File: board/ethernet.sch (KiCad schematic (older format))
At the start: 1 part

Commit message: Roughed out ethernet sheet
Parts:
- added C? (x4): 10n 200V, agg:0805, symbol C
- added C? (x5): 100n, agg:0603, symbol C
- added C? (x2): 30p, agg:0603, symbol C
- added C?: 2u2, agg:0603, symbol C
- added C? (x2): 22u, agg:1206, symbol C
- added C?: C, agg:0603, symbol C
- added C?: 100n 60V, agg:0805, symbol C
- added C? (x6): C, symbol C
- added D?: 1N4148, agg:SOD-323, symbol D
- added D? (x8): SS110B, agg:DO-214AA-SMB, symbol D
- added D?: SMAJ58A, agg:DO-214AC-SMA, symbol ZENERsmall
- added IC?: KSZ8081RNx, agg:QFN-24-EP-MICREL, symbol KSZ8081RNx
- added IC?: MAX5969x, agg:DFN-10-EP-MAX, symbol MAX5969x
- added IC?: MAX17503, agg:QFN-20-EP-MAX, symbol MAX17503
- added L?: FB, agg:0603, symbol L_Small
- added L?: 3u3, symbol INDUCTOR
- added L?: INDUCTOR, symbol INDUCTOR
- added R? (x4): 75, agg:0603, symbol R
- added R? (x4): 33, agg:0603, symbol R_Small
- added R?: 1k, agg:0603, symbol R_Small
- added R?: 6k49, agg:0603, symbol R
- added R?: 10k, agg:0603, symbol R
- added R? (x2): 1k, agg:0603, symbol R
- added R?: 24k9, agg:0603, symbol R_Small
- added R?: 619, agg:0603, symbol R_Small
- added R?: 3M3, symbol R_Small
- added R? (x2): R, symbol R
- added T?: 749010012A, agg:749010012A, symbol 749010012A
- added Y?: 25MHz, agg:XTAL-50x32, symbol Crystal
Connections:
- net +48V: now also C?.1, IC?.1 (VIN), IC?.2 (VIN), IC?.3 (VIN), L?.1, R?.1
- net CRS_DV: now also R?.1
- net MDC: now also IC?.11 (MDC)
- net MDIO: now also IC?.10 (MDIO), R?.2
- net REF_CLK: now also R?.1
- net RXD0: now also R?.1
- net RXD1: now also R?.1
- net TXD0: now also IC?.20 (TXD0)
- net TXD1: now also IC?.21 (TXD1)
- net TXEN: now also IC?.19 (TXEN)
- net at J?.1: now also T?.8 (TD+)
- net at J?.10: now also R?.2
- net TRAFFIC_LED: now reaches J?.11
- net at J?.12: now also R?.1
- net at J?.2: now also T?.6 (TD-)
- net at J?.3: now also T?.3 (RD+)
- net VB2: now reaches J?.4
- net VB2: now also J?.5, C?.1, C?.1, D?.1 (K), D?.1 (K), D?.2 (A)
- net at J?.6: now also T?.1 (RD-)
- net VB1: now reaches J?.7
- net VB1: now also J?.8, C?.1, D?.1 (K), D?.2 (A)
- net LINK_LED: now reaches J?.9
- net LINK_LED: now also IC?.23 (LED0)
- new net: C?.1, T?.10 (CTX)
- new net: IC?.5 (TXM), T?.11 (TX-)
- new net: IC?.4 (RXP), T?.14 (RX+)
- new net: C?.1, T?.15 (CRX)
- new net: IC?.3 (RXM), T?.16 (RX-)
- new net: C?.1, T?.2 (CRD)
- new net: C?.1, T?.7 (CTD)
- new net: IC?.6 (TXP), T?.9 (TX+)
- new net: C?.1, C?.1, IC?.1 (VDD_1v2)
- new net: IC?.12 (RXD1), R?.2
- new net: IC?.13 (RXD0), R?.2
- new net: IC?.15 (CRS_DV), R?.2
- new net: IC?.16 (REF_CLK), R?.2
- new net: C?.1, C?.1, IC?.2 (VDDA_3v3), L?.1
- new net: C?.1, D?.2 (A), IC?.24 (~RST), R?.2
- new net: C?.1, IC?.7 (XO), Y?.2
- new net: C?.1, IC?.8 (XI), Y?.1
- new net: IC?.9 (REXT), R?.1
- new net: D?.1 (K), D?.1 (K), D?.1 (K), D?.1 (K), IC?.1 (VDD), L?.2, R?.2
- new net: IC?.10 (CLS), R?.1
- new net: IC?.2 (DET), R?.1
- new net: C?.2, D?.2 (A), D?.2 (A), D?.2 (A), D?.2 (A), D?.2 (A), IC?.5 (VSS), IC?.EP (VSS), R?.2
- new net: C?.1, IC?.12 (VCC)
- new net: C?.2, IC?.17 (LX), IC?.18 (LX), IC?.19 (LX), L?.2
- new net: C?.1, IC?.20 (BST)
- new net: C?.1, IC?.7 (SS)
- new net: IC?.9 (FB), R?.1, R?.2
- new net: C?.2, R?.1 (x4)
- new net: R?.2, R?.2, R?.2, R?.2
- new net +12V: C?.1, C?.1, L?.1, R?.1
- new net +3V3: C?.1, C?.1, D?.1 (K), IC?.14 (VDDIO), L?.2, R?.1, R?.1, R?.1, R?.2
- new net GND: C?.2, C?.2, C?.2, C?.2, C?.2, C?.2, C?.2, C?.2, C?.2, C?.2, C?.2, C?.2, C?.2, C?.2, C?.2, C?.2, IC?.11 (MODE), IC?.13 (SGND), IC?.14 (PGND), IC?.15 (PGND), IC?.16 (PGND), IC?.22 (GND), IC?.6 (RTN), IC?.7 (WAD), IC?.EP (GND), IC?.EP (SGND), R?.2, R?.2
- new net POE_GOOD: IC?.4 (EN/UVLO), IC?.8 (PG), R?.2
- new net VA1: D?.1 (K), D?.2 (A)
- new net VA2: D?.1 (K), D?.2 (A)
- no-connect marks 0 -> 7
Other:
- moved on the sheet: J?

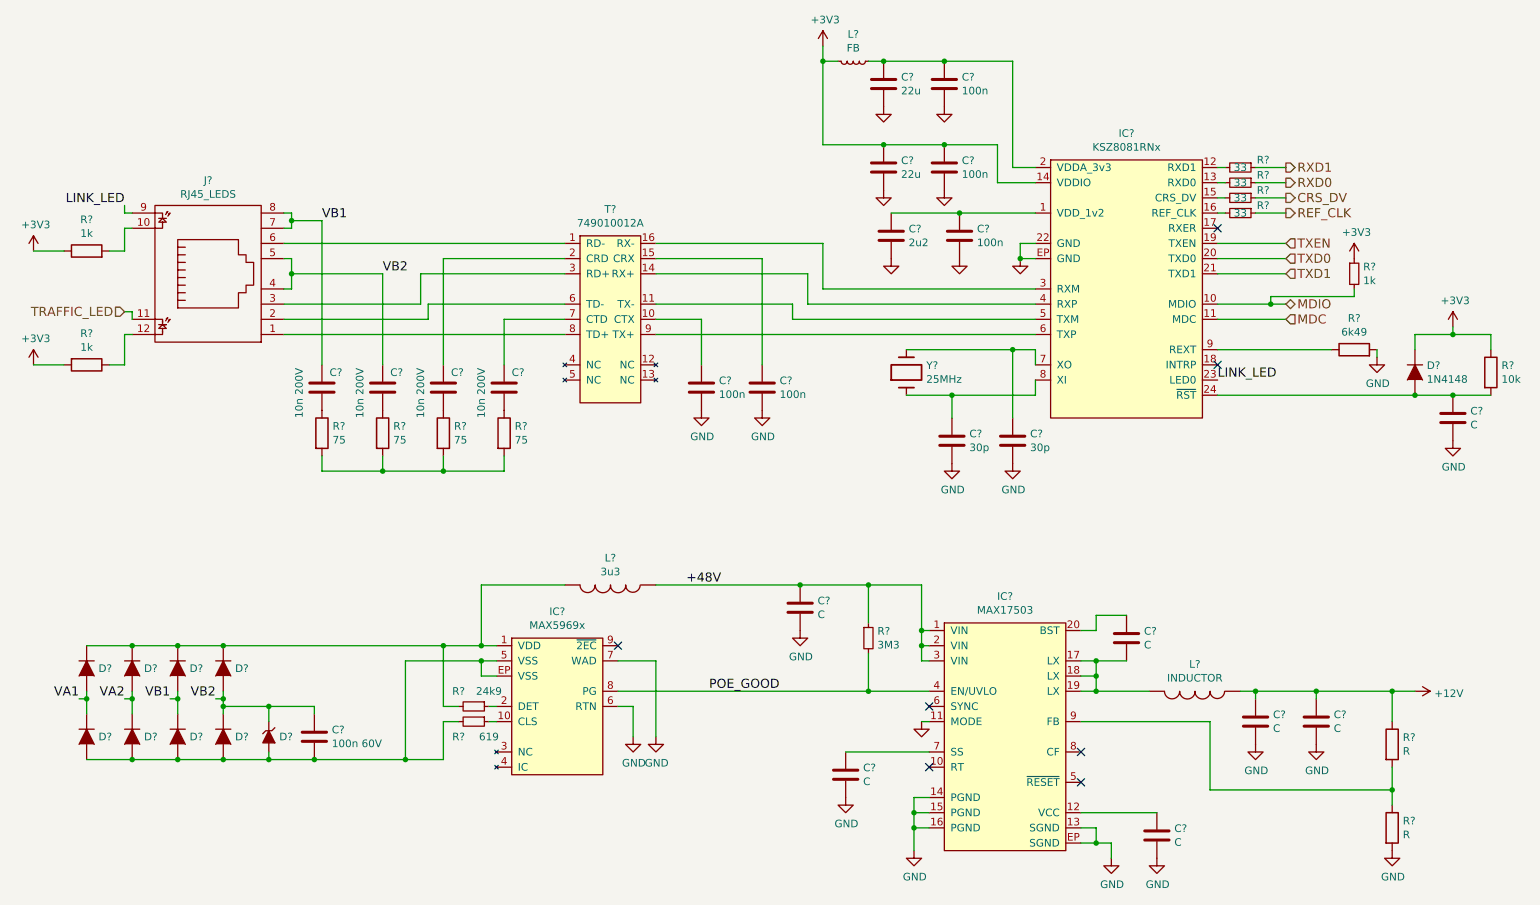
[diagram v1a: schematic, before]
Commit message: Values for ethernet and max17503
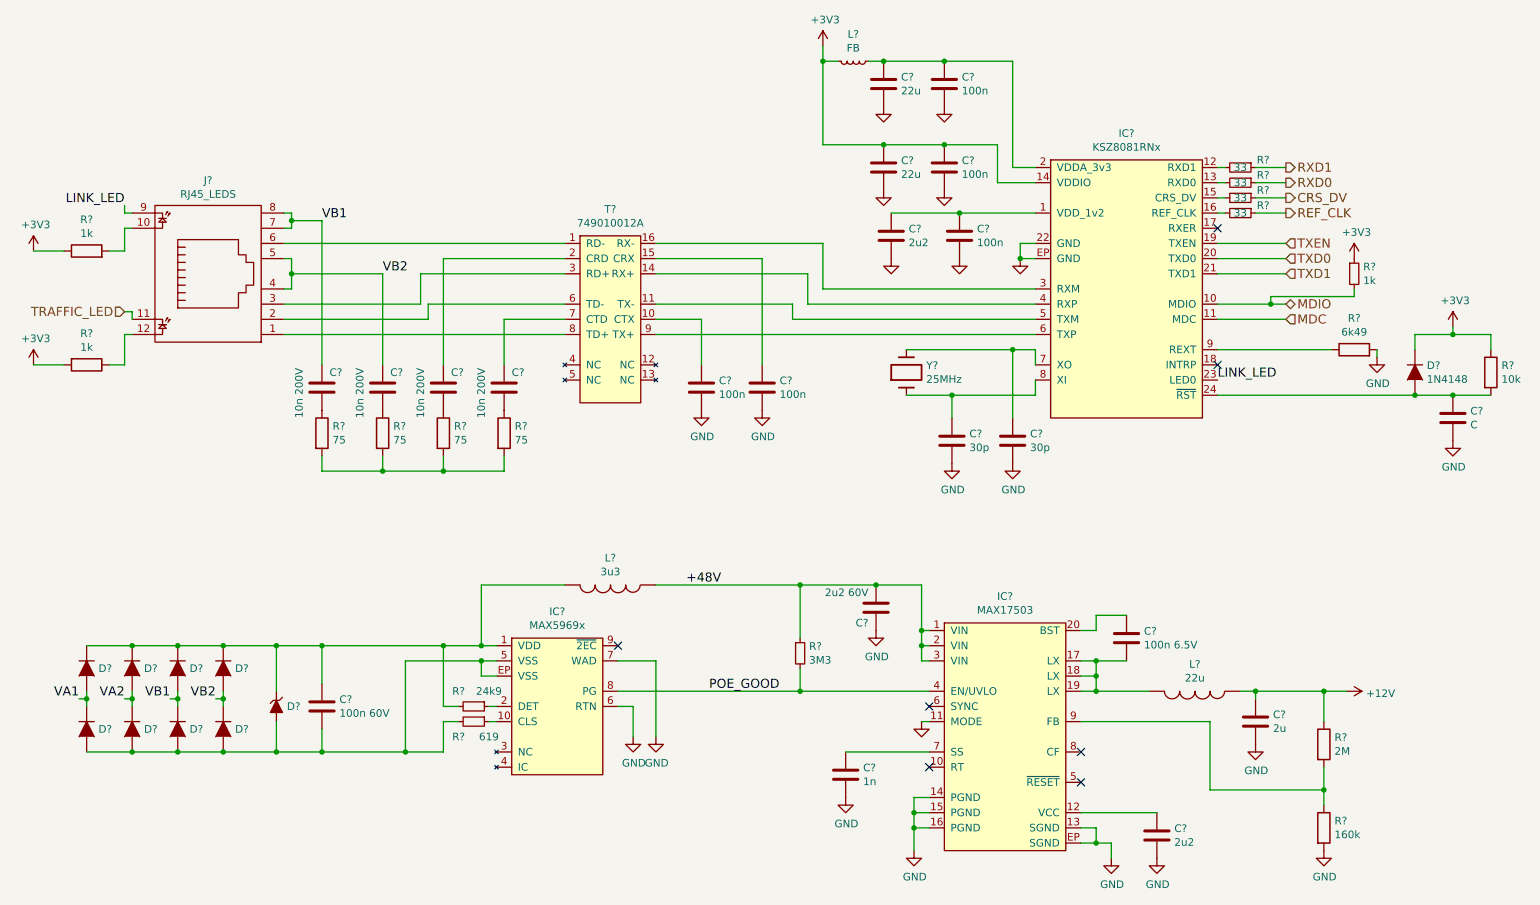
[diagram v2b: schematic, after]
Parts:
- removed C?: C, symbol C
- C?: value C -> 2u2 60V; footprint (none) -> agg:1210
- C?: value C -> 1n; footprint (none) -> agg:0603
- C?: value C -> 100n 6.5V; footprint (none) -> agg:0603
- C?: value C -> 2u2; footprint (none) -> agg:0603
- C?: value C -> 2u; footprint (none) -> agg:1206
- L?: value 3u3 -> 22u; footprint (none) -> footprints:SRR1260A; Farnell (none) -> 1929699
- L?: value INDUCTOR -> 3u3; footprint (none) -> footprints:ELLATP3R3NB; Farnell (none) -> 1865686
- R?: footprint (none) -> agg:0603
- R?: value R -> 2M; footprint (none) -> agg:0603; Farnell (none) -> 2059687
- R?: value R -> 160k; footprint (none) -> agg:0603; Farnell (none) -> 2670652
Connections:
- net +12V: now also L?.1; no longer L?.1
- net +48V: now also C?.2, L?.1; no longer C?.1, L?.1
- net GND: now also C?.1; no longer C?.2
- net VB2: no longer C?.1, D?.1 (K)
- net at D?.1 (K), D?.1 (K), D?.1 (K)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: now also C?.1, D?.1 (K), L?.2; no longer L?.2
- net at C?.2, IC?.17 (LX), IC?.18 (LX)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: now also L?.2; no longer L?.2
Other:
- moved on the sheet: C?, D?, L?, R?

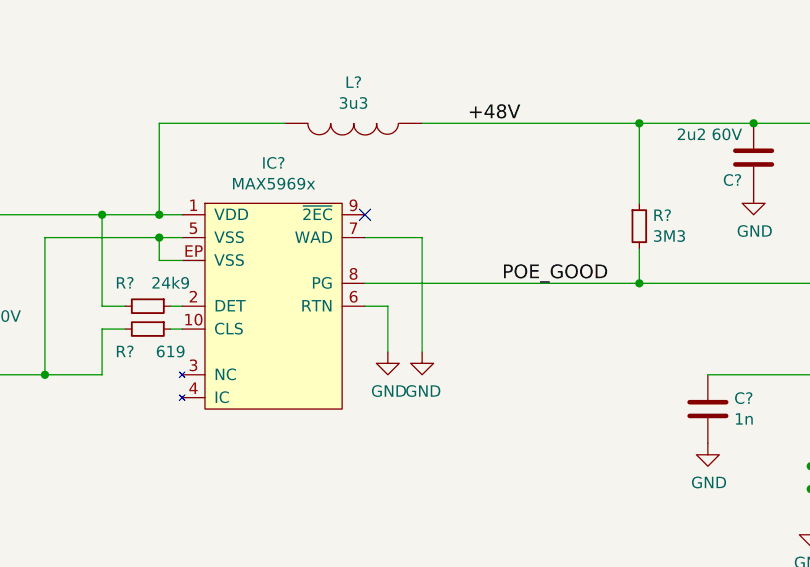
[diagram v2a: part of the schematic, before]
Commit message: STM32 support and 25EE MAC chip
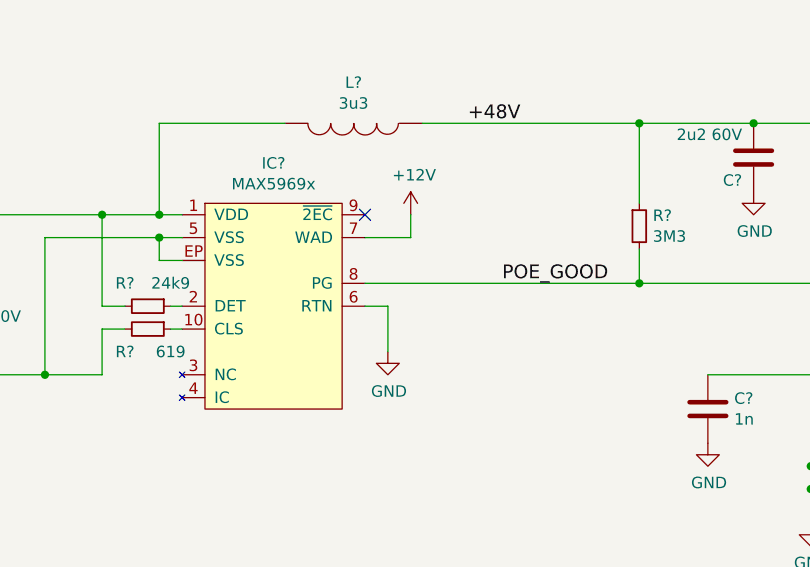
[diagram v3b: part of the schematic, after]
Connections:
- net +12V: now also IC?.7 (WAD)
- net GND: no longer IC?.7 (WAD)
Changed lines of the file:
@@
 LIBS:max5969x
 LIBS:max17503
+LIBS:stm32f4xxvxtx
+LIBS:smd_xtal
+LIBS:swd
+LIBS:swd_tc
+LIBS:25aa02e48
 LIBS:bigtime-cache
 EELAYER 26 0
@@
 $EndComp
 $Comp
-L GND #PWR?
-U 1 1 58BC4BAF
-P 4950 5300
-F 0 "#PWR?" H 4950 5050 50  0001 C CNN
-F 1 "GND" H 4955 5127 50  0000 C CNN
-F 2 "" H 4950 5300 50  0000 C CNN
-F 3 "" H 4950 5300 50  0000 C CNN
-	1    4950 5300
-	1    0    0    -1
-$EndComp
-$Comp
 L C C?
 U 1 1 58BC71FE
@@
 	4800 5100 4800 5300
 Wire Wire Line
-	4700 4800 4950 4800
-Wire Wire Line
-	4950 4800 4950 5300
-Wire Wire Line
 	4700 5000 6750 5000
 Wire Wire Line
@@
 Wire Wire Line
 	9350 5650 8600 5650
+$Comp
+L +12V #PWR?
+U 1 1 58BC71BD
+P 4900 4700
+F 0 "#PWR?" H 4900 4550 50  0001 C CNN
+F 1 "+12V" H 4915 4873 50  0000 C CNN
+F 2 "" H 4900 4700 50  0000 C CNN
+F 3 "" H 4900 4700 50  0000 C CNN
+	1    4900 4700
+	1    0    0    -1
+$EndComp
+Wire Wire Line
+	4900 4700 4900 4800
+Wire Wire Line
+	4900 4800 4700 4800
 $EndSCHEMATC

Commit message: test points, footprints, usb
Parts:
- added TP3: +48V, agg:SIL-254P-01, symbol TEST
- added TP4: +12V, agg:SIL-254P-01, symbol TEST
- added TP5: POE_GOOD, agg:SIL-254P-01, symbol TEST
- J1: renamed from J?; footprint (none) -> Connect:RJHSE538X
- gave numbers to parts that had none: 57
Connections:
- wire segments 157 -> 160

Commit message: Specced part for brightness trimpot
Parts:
- TP3, TP4, TP5: symbol TEST -> TEST-RESCUE-bigtime
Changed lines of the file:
@@
 TRAFFIC_LED
 $Comp
-L +3V3 #PWR037
+L +3V3 #PWR38
 U 1 1 58B9F15A
 P 850 2850
-F 0 "#PWR037" H 850 2700 50  0001 C CNN
+F 0 "#PWR38" H 850 2700 50  0001 C CNN
 F 1 "+3V3" H 865 3023 50  0000 C CNN
 F 2 "" H 850 2850 50  0000 C CNN
@@
 LINK_LED
 $Comp
-L +3V3 #PWR038
+L +3V3 #PWR37
 U 1 1 58B9F35C
 P 850 2100
-F 0 "#PWR038" H 850 1950 50  0001 C CNN
+F 0 "#PWR37" H 850 1950 50  0001 C CNN
 F 1 "+3V3" H 865 2273 50  0000 C CNN
 F 2 "" H 850 2100 50  0000 C CNN
@@
 $EndComp
 $Comp
-L GND #PWR039
+L GND #PWR41
 U 1 1 58BA0647
 P 5250 3150
-F 0 "#PWR039" H 5250 2900 50  0001 C CNN
+F 0 "#PWR41" H 5250 2900 50  0001 C CNN
 F 1 "GND" H 5255 2977 50  0000 C CNN
 F 2 "" H 5250 3150 50  0000 C CNN
@@
 $EndComp
 $Comp
-L GND #PWR040
+L GND #PWR42
 U 1 1 58BA068E
 P 5650 3150
-F 0 "#PWR040" H 5650 2900 50  0001 C CNN
+F 0 "#PWR42" H 5650 2900 50  0001 C CNN
 F 1 "GND" H 5655 2977 50  0000 C CNN
 F 2 "" H 5650 3150 50  0000 C CNN
@@
 $EndComp
 $Comp
-L GND #PWR041
+L GND #PWR56
 U 1 1 58BA115A
 P 7350 2150
-F 0 "#PWR041" H 7350 1900 50  0001 C CNN
+F 0 "#PWR56" H 7350 1900 50  0001 C CNN
 F 1 "GND" H 7355 1977 50  0001 C CNN
 F 2 "" H 7350 2150 50  0000 C CNN
@@
 $EndComp
 $Comp
-L GND #PWR042
+L GND #PWR53
 U 1 1 58BA1640
 P 6900 3500
-F 0 "#PWR042" H 6900 3250 50  0001 C CNN
+F 0 "#PWR53" H 6900 3250 50  0001 C CNN
 F 1 "GND" H 6905 3327 50  0000 C CNN
 F 2 "" H 6900 3500 50  0000 C CNN
@@
 $EndComp
 $Comp
-L GND #PWR043
+L GND #PWR55
 U 1 1 58BA1690
 P 7300 3500
-F 0 "#PWR043" H 7300 3250 50  0001 C CNN
+F 0 "#PWR55" H 7300 3250 50  0001 C CNN
 F 1 "GND" H 7305 3327 50  0000 C CNN
 F 2 "" H 7300 3500 50  0000 C CNN
@@
 $EndComp
 $Comp
-L GND #PWR044
+L GND #PWR48
 U 1 1 58BA1A5E
 P 6500 2150
-F 0 "#PWR044" H 6500 1900 50  0001 C CNN
+F 0 "#PWR48" H 6500 1900 50  0001 C CNN
 F 1 "GND" H 6505 1977 50  0001 C CNN
 F 2 "" H 6500 2150 50  0000 C CNN
@@
 $EndComp
 $Comp
-L GND #PWR045
+L GND #PWR54
 U 1 1 58BA1AB4
 P 6950 2150
-F 0 "#PWR045" H 6950 1900 50  0001 C CNN
+F 0 "#PWR54" H 6950 1900 50  0001 C CNN
 F 1 "GND" H 6955 1977 50  0001 C CNN
 F 2 "" H 6950 2150 50  0000 C CNN
@@
 $EndComp
 $Comp
-L +3V3 #PWR046
+L +3V3 #PWR43
 U 1 1 58BA1E02
 P 6050 750
-F 0 "#PWR046" H 6050 600 50  0001 C CNN
+F 0 "#PWR43" H 6050 600 50  0001 C CNN
 F 1 "+3V3" H 6065 923 50  0000 C CNN
 F 2 "" H 6050 750 50  0000 C CNN
@@
 $EndComp
 $Comp
-L GND #PWR047
+L GND #PWR46
 U 1 1 58BA48D5
 P 6450 1150
-F 0 "#PWR047" H 6450 900 50  0001 C CNN
+F 0 "#PWR46" H 6450 900 50  0001 C CNN
 F 1 "GND" H 6455 977 50  0001 C CNN
 F 2 "" H 6450 1150 50  0000 C CNN
@@
 $EndComp
 $Comp
-L GND #PWR048
+L GND #PWR51
 U 1 1 58BA492B
 P 6850 1150
-F 0 "#PWR048" H 6850 900 50  0001 C CNN
+F 0 "#PWR51" H 6850 900 50  0001 C CNN
 F 1 "GND" H 6855 977 50  0001 C CNN
 F 2 "" H 6850 1150 50  0000 C CNN
@@
 $EndComp
 $Comp
-L GND #PWR049
+L GND #PWR47
 U 1 1 58BA4B25
 P 6450 1700
-F 0 "#PWR049" H 6450 1450 50  0001 C CNN
+F 0 "#PWR47" H 6450 1450 50  0001 C CNN
 F 1 "GND" H 6455 1527 50  0001 C CNN
 F 2 "" H 6450 1700 50  0000 C CNN
@@
 $EndComp
 $Comp
-L GND #PWR050
+L GND #PWR52
 U 1 1 58BA4BE5
 P 6850 1700
-F 0 "#PWR050" H 6850 1450 50  0001 C CNN
+F 0 "#PWR52" H 6850 1450 50  0001 C CNN
 F 1 "GND" H 6855 1527 50  0001 C CNN
 F 2 "" H 6850 1700 50  0000 C CNN
@@
 $EndComp
 $Comp
-L +3V3 #PWR051
+L +3V3 #PWR61
 U 1 1 58BA8C0B
 P 9550 2150
-F 0 "#PWR051" H 9550 2000 50  0001 C CNN
+F 0 "#PWR61" H 9550 2000 50  0001 C CNN
 F 1 "+3V3" H 9565 2323 50  0000 C CNN
 F 2 "" H 9550 2150 50  0000 C CNN
@@
 $EndComp
 $Comp
-L GND #PWR052
+L GND #PWR62
 U 1 1 58BABD3E
 P 9700 2800
-F 0 "#PWR052" H 9700 2550 50  0001 C CNN
+F 0 "#PWR62" H 9700 2550 50  0001 C CNN
 F 1 "GND" H 9705 2627 50  0000 C CNN
 F 2 "" H 9700 2800 50  0000 C CNN
@@
 $EndComp
 $Comp
-L +3V3 #PWR053
+L +3V3 #PWR64
 U 1 1 58BAD620
 P 10200 2600
-F 0 "#PWR053" H 10200 2450 50  0001 C CNN
+F 0 "#PWR64" H 10200 2450 50  0001 C CNN
 F 1 "+3V3" H 10215 2773 50  0000 C CNN
 F 2 "" H 10200 2600 50  0000 C CNN
@@
 $EndComp
 $Comp
-L GND #PWR054
+L GND #PWR65
 U 1 1 58BAD7C0
 P 10200 3350
-F 0 "#PWR054" H 10200 3100 50  0001 C CNN
+F 0 "#PWR65" H 10200 3100 50  0001 C CNN
 F 1 "GND" H 10205 3177 50  0000 C CNN
 F 2 "" H 10200 3350 50  0000 C CNN
@@
 NoConn ~ 4700 4700
 $Comp
-L GND #PWR055
+L GND #PWR39
 U 1 1 58BC4A36
 P 4800 5300
-F 0 "#PWR055" H 4800 5050 50  0001 C CNN
+F 0 "#PWR39" H 4800 5050 50  0001 C CNN
 F 1 "GND" H 4805 5127 50  0000 C CNN
 F 2 "" H 4800 5300 50  0000 C CNN
@@
 $EndComp
 $Comp
-L GND #PWR056
+L GND #PWR45
 U 1 1 58BC73C0
 P 6400 4600
-F 0 "#PWR056" H 6400 4350 50  0001 C CNN
+F 0 "#PWR45" H 6400 4350 50  0001 C CNN
 F 1 "GND" H 6405 4427 50  0000 C CNN
 F 2 "" H 6400 4600 50  0000 C CNN
@@
 NoConn ~ 6750 5100
 $Comp
-L GND #PWR057
+L GND #PWR50
 U 1 1 58BC9E72
 P 6700 5200
-F 0 "#PWR057" H 6700 4950 50  0001 C CNN
+F 0 "#PWR50" H 6700 4950 50  0001 C CNN
 F 1 "GND" H 6705 5027 50  0001 C CNN
 F 2 "" H 6700 5200 50  0000 C CNN
@@
 $EndComp
 $Comp
-L GND #PWR058
+L GND #PWR44
 U 1 1 58BCA458
 P 6200 5700
-F 0 "#PWR058" H 6200 5450 50  0001 C CNN
+F 0 "#PWR44" H 6200 5450 50  0001 C CNN
 F 1 "GND" H 6205 5527 50  0000 C CNN
 F 2 "" H 6200 5700 50  0000 C CNN
@@
 NoConn ~ 6750 5500
 $Comp
-L GND #PWR059
+L GND #PWR49
 U 1 1 58BCAA6F
 P 6650 6050
-F 0 "#PWR059" H 6650 5800 50  0001 C CNN
+F 0 "#PWR49" H 6650 5800 50  0001 C CNN
 F 1 "GND" H 6655 5877 50  0000 C CNN
 F 2 "" H 6650 6050 50  0000 C CNN
@@
 NoConn ~ 7750 5600
 $Comp
-L GND #PWR060
+L GND #PWR57
 U 1 1 58BCCF2C
 P 7950 6100
-F 0 "#PWR060" H 7950 5850 50  0001 C CNN
+F 0 "#PWR57" H 7950 5850 50  0001 C CNN
 F 1 "GND" H 7955 5927 50  0000 C CNN
 F 2 "" H 7950 6100 50  0000 C CNN
@@
 $EndComp
 $Comp
-L GND #PWR061
+L GND #PWR58
 U 1 1 58BCD1A4
 P 8250 6100
-F 0 "#PWR061" H 8250 5850 50  0001 C CNN
+F 0 "#PWR58" H 8250 5850 50  0001 C CNN
 F 1 "GND" H 8255 5927 50  0000 C CNN
 F 2 "" H 8250 6100 50  0000 C CNN
@@
 $EndComp
 $Comp
-L GND #PWR062
+L GND #PWR59
 U 1 1 58BCDD4D
 P 8900 5350
-F 0 "#PWR062" H 8900 5100 50  0001 C CNN
+F 0 "#PWR59" H 8900 5100 50  0001 C CNN
 F 1 "GND" H 8905 5177 50  0000 C CNN
 F 2 "" H 8900 5350 50  0000 C CNN
@@
 $EndComp
 $Comp
-L GND #PWR063
+L GND #PWR60
 U 1 1 58BCE5C3
 P 9350 6050
-F 0 "#PWR063" H 9350 5800 50  0001 C CNN
+F 0 "#PWR60" H 9350 5800 50  0001 C CNN
 F 1 "GND" H 9355 5877 50  0000 C CNN
 F 2 "" H 9350 6050 50  0000 C CNN
@@
 $EndComp
 $Comp
-L +12V #PWR064
+L +12V #PWR63
 U 1 1 58BCF882
 P 9800 5000
-F 0 "#PWR064" H 9800 4850 50  0001 C CNN
+F 0 "#PWR63" H 9800 4850 50  0001 C CNN
 F 1 "+12V" V 9815 5128 50  0000 L CNN
 F 2 "" H 9800 5000 50  0000 C CNN
@@
 	9350 5650 8600 5650
 $Comp
-L +12V #PWR065
+L +12V #PWR40
 U 1 1 58BC71BD
 P 4900 4700
-F 0 "#PWR065" H 4900 4550 50  0001 C CNN
+F 0 "#PWR40" H 4900 4550 50  0001 C CNN
 F 1 "+12V" H 4915 4873 50  0000 C CNN
 F 2 "" H 4900 4700 50  0000 C CNN
@@
 VA2
 $Comp
-L TEST TP3
+L TEST-RESCUE-bigtime TP3
 U 1 1 58D5FB4B
 P 5650 4200
+AR Path="/58D5FB4B" Ref="TP3"  Part="1"
+AR Path="/58B736A9/58D5FB4B" Ref="TP3"  Part="1"
 F 0 "TP3" H 5728 4340 50  0000 L CNN
 F 1 "+48V" H 5728 4249 50  0000 L CNN
@@
 Connection ~ 5650 4300
 $Comp
-L TEST TP4
+L TEST-RESCUE-bigtime TP4
 U 1 1 58D6337D
 P 9600 4850
+AR Path="/58D6337D" Ref="TP4"  Part="1"
+AR Path="/58B736A9/58D6337D" Ref="TP4"  Part="1"
 F 0 "TP4" H 9678 4990 50  0000 L CNN
 F 1 "+12V" H 9678 4899 50  0000 L CNN
@@
 Connection ~ 9600 5000
 $Comp
-L TEST TP5
+L TEST-RESCUE-bigtime TP5
 U 1 1 58D6A1A7
 P 5200 5100
+AR Path="/58D6A1A7" Ref="TP5"  Part="1"
+AR Path="/58B736A9/58D6A1A7" Ref="TP5"  Part="1"
 F 0 "TP5" H 5122 5147 50  0000 R CNN
 F 1 "POE_GOOD" H 5122 5238 50  0000 R CNN
